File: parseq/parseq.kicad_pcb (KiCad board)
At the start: 2 copper layers, 47.5 x 55 mm, 46 parts, among them J1 Conn_01x01, J2 Conn_01x01, J3 Conn_01x01, J4 Conn_01x01, U1 Opamp_Quad, U2 Opamp_Dual

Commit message: .
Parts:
- moved R18 14.5 mm to (159.5, 102.5), turned to 90 degrees
- moved R19 8.33 mm to (140.4, 79.2), turned to -90 degrees
- moved RV3 0.15 mm to (178.5, 89.5)
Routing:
- net Net-(R18-Pad2): track 60.6 -> 26.2 mm
- net Net-(C7-Pad1): track 95.7 -> 64.9 mm
- net Net-(C11-Pad2): track 37.0 -> 25.8 mm
- net GND: track 0.00 -> 7.43 mm
- net Net-(C11-Pad1): track 7.64 -> 13.2 mm
- net Net-(U1B-+): track 36.9 -> 39.6 mm
- net Net-(C8-Pad1): track 8.20 -> 10.7 mm
- net Net-(U1C--): track 61.8 -> 64.2 mm
- net Net-(R17-Pad1): track 33.1 -> 31.4 mm
- net Net-(C12-Pad1): track 22.4 -> 23.2 mm
- net Net-(C9-Pad1): track 42.3 -> 41.7 mm
- net Net-(RV1A-6): track 41.3 -> 41.8 mm

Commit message: update board
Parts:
- removed R14: 100, 1_trevortjes_lib:R_1x4
- added C13: 100u, 1_trevortjes_lib:CP_ELCO_1x2_S, F.Cu at (141.6, 84.7)
- added R22: 100, 1_trevortjes_lib:R_1x4, F.Cu at (154.7, 76.8)
- added R23: 100, 1_trevortjes_lib:R_1x4, F.Cu at (156.2, 83.9)
- C2: moved to B.Cu
- C8: moved to F.Cu
- moved R15 44.3 mm to (155.1, 62.9), turned to 0 degrees
- moved J4 36.6 mm to (180.8, 77.4)
- moved R10 36.0 mm to (167.6, 111.5), turned to 90 degrees
- moved R16 28.5 mm to (163.8, 90.5), turned to 180 degrees
- moved R11 27.7 mm to (145.7, 106.8), turned to 180 degrees
- moved R17 26.2 mm to (137.0, 76.8)
- moved C2 24.8 mm to (150.8, 89.4), turned to 0 degrees
- moved J3 24.2 mm to (137.6, 89.8), turned to 180 degrees
- moved R4 23.5 mm to (155.3, 106.8), turned to 0 degrees
- moved R18 23.4 mm to (152.6, 80.2), turned to 0 degrees
- moved C8 23.1 mm to (149.8, 80.2), turned to 180 degrees
- moved R1 21.5 mm to (156.2, 87.1)
- moved R13 20.7 mm to (172.2, 106.8), turned to 0 degrees
- moved C6 20.6 mm to (175.0, 78.6)
- moved U1 20.6 mm to (169.8, 78.6)
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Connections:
- C5 pad 1: Net-(U1A-+) -> Net-(U1C-+)
- C5 pad 2: Net-(U1B-+) -> Net-(U1B--)
- C7 pad 2: Net-(U1A--) -> Net-(U1C--)
- R10 pad 2: Net-(U1A--) -> Net-(U1C--)
- R11 pad 1: Net-(U1C--) -> Net-(U1A-+)
- R13 pad 2: Net-(U1C-+) -> Net-(U1A--)
- R15 pad 1: Net-(U1E-V+) -> Net-(D1-K)
- R4 pad 1: Net-(U1C--) -> Net-(U1A-+)
- R4 pad 2: Net-(U1A-+) -> Net-(U1C-+)
- R5 pad 1: Net-(U1C-+) -> Net-(U1A--)
- R6 pad 1: Net-(U1C-+) -> Net-(U1A--)
- R7 pad 2: Net-(U1B-+) -> Net-(U1B--)
- R9 pad 1: Net-(U1A--) -> Net-(U1C--)
- RV1 pad 6: Net-(U1A-+) -> Net-(U1C-+)
- RV3 pad 3: Net-(U1C--) -> Net-(U1A-+)
- U1 pad 1: Net-(C7-Pad1) -> Net-(RV1A-6)
- U1 pad 5: Net-(U1B-+) -> /vref
- U1 pad 6: /vref -> Net-(U1B--)
- U1 pad 7: Net-(U1A-+) -> Net-(U1C-+)
- U1 pad 8: Net-(RV1A-6) -> Net-(C7-Pad1)
- U2 pad 8: Net-(U1E-V+) -> Net-(U2C-V+)
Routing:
- net Net-(U1C--): track 64.2 -> 21.7 mm
- net Net-(U1A-+): track 38.7 -> 80.0 mm
- net Net-(U1B-+): track 39.6 -> 0.00 mm
- net Net-(J4-Pin_1): track 42.2 -> 6.78 mm
- net Net-(C12-Pad1): track 23.2 -> 52.3 mm
- net Net-(R17-Pad1): track 31.4 -> 7.01 mm
- net Net-(D1-K): track 3.07 -> 26.7 mm
- net Net-(U1E-V+): track 32.1 -> 11.4 mm
- net Net-(R18-Pad2): track 26.2 -> 6.94 mm
- net Net-(C7-Pad1): track 64.9 -> 83.2 mm
- net Net-(J3-Pin_1): track 3.56 -> 17.1 mm
- net Net-(RV1A-6): track 41.8 -> 54.6 mm
- net Net-(U2C-V+): track 0.00 -> 12.1 mm
- net Net-(U1B--): track 0.00 -> 12.1 mm
- net Net-(C11-Pad2): track 25.8 -> 17.5 mm
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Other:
- board size 47.5 x 55 mm -> 47.5 x 54.6 mm
- board text added: "125b between screws (in long dimension)"

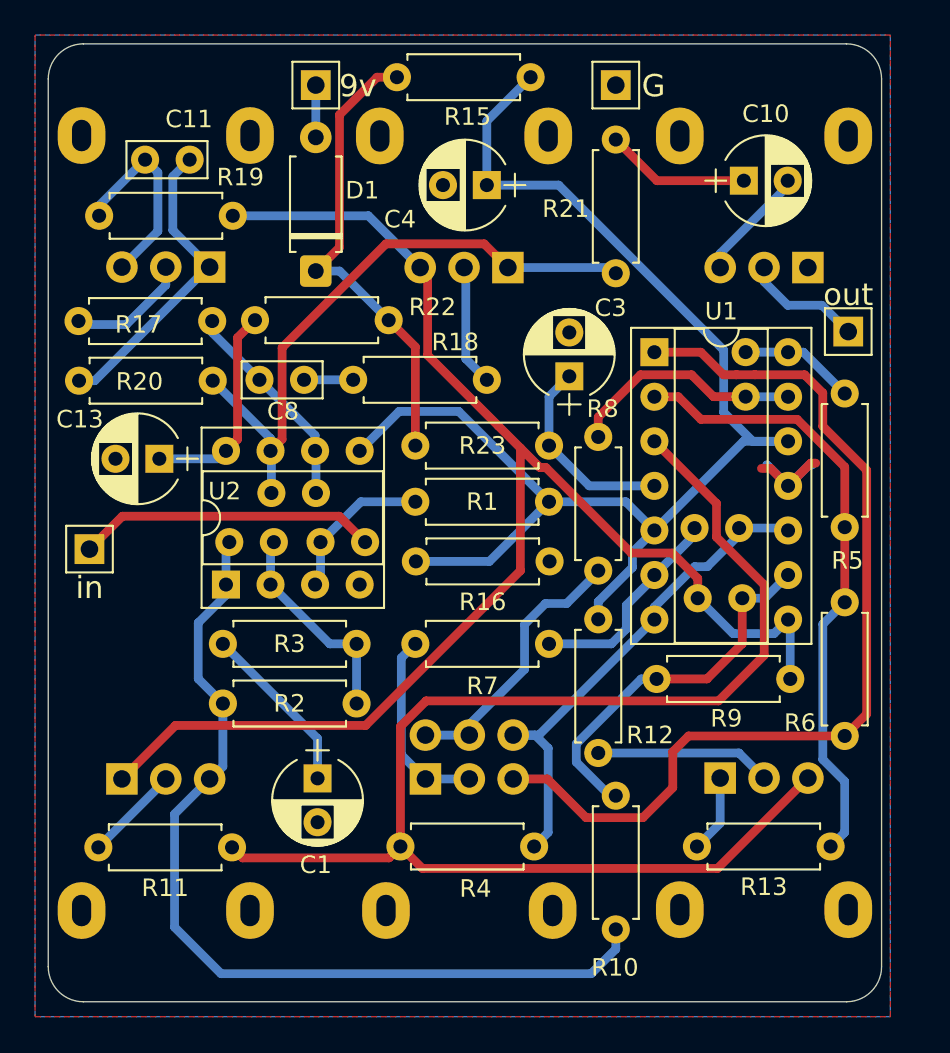
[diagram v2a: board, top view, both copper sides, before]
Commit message: shorter tracks
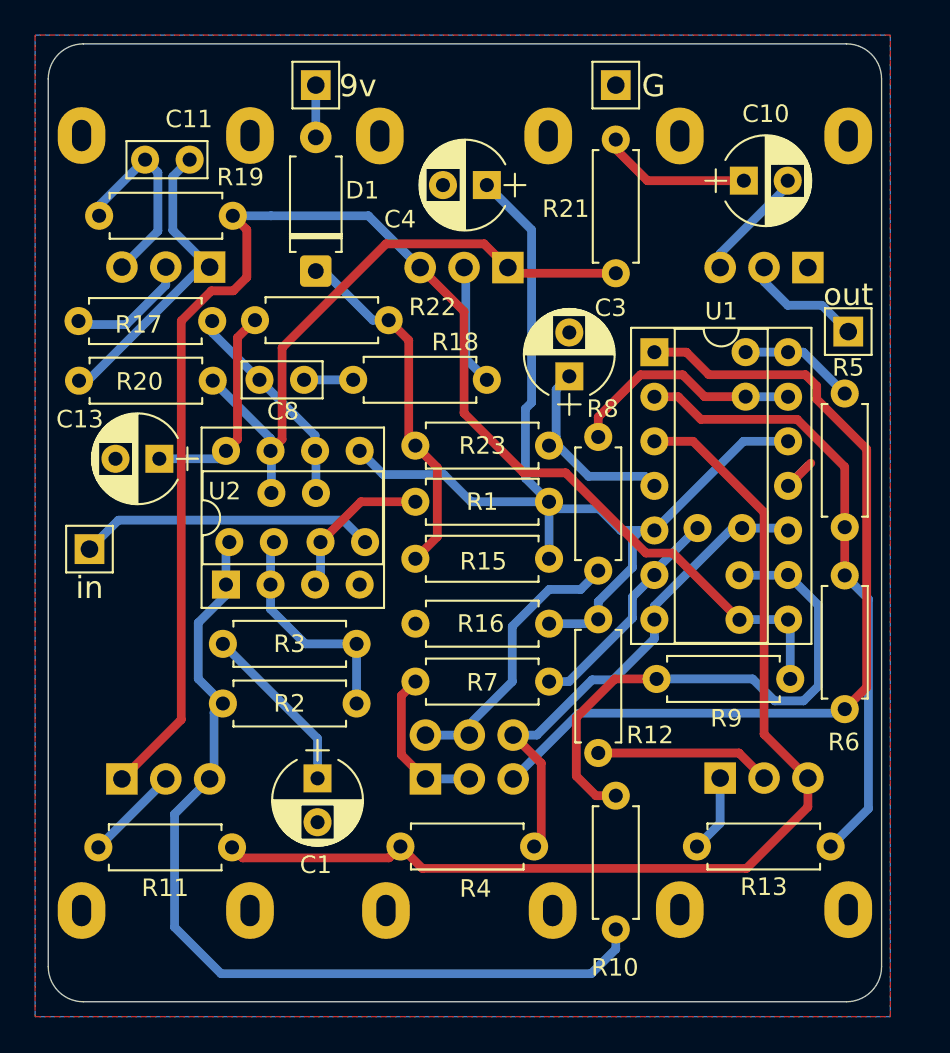
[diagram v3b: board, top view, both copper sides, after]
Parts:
- moved R15 27.5 mm to (156.2, 90.3)
- moved R16 8.43 mm to (156.2, 94.0), turned to 0 degrees
- moved C7 2.68 mm to (174.7, 93.8), turned to 90 degrees
- moved R7 2.15 mm to (156.2, 97.3)
- moved R6 1.53 mm to (180.7, 91.3)
- moved C5 0.17 mm to (174.8, 88.6)
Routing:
- net Net-(U1A-+): track 80.0 -> 61.1 mm
- net /vref: track 78.1 -> 61.2 mm
- net Net-(U1C--): track 21.7 -> 31.5 mm
- net Net-(D1-K): track 26.7 -> 20.6 mm
- net GND: track 7.64 -> 3.52 mm
- net Net-(RV1A-6): track 54.6 -> 50.7 mm
- net Net-(RV1A-4): track 11.1 -> 8.95 mm
- net Net-(C7-Pad1): track 83.2 -> 84.2 mm
- net Net-(U2A--): track 12.2 -> 13.0 mm
- net Net-(U1B--): track 12.1 -> 12.9 mm
- net Net-(U1C-+): track 29.5 -> 28.9 mm

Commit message: add name and version to silkscreen
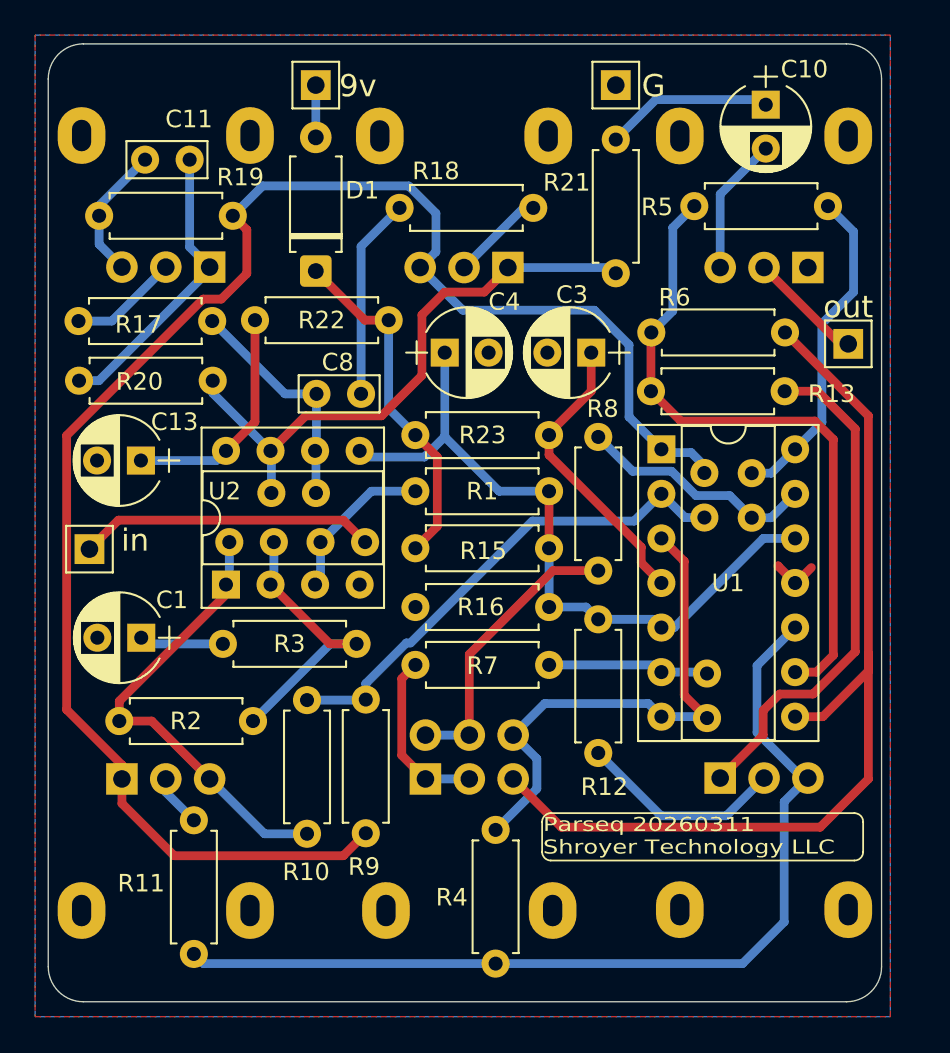
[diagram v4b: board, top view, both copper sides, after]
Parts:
- moved R13 26.4 mm to (177.2, 80.8), turned to 180 degrees
- moved R5 20.2 mm to (172.1, 70.2), turned to 0 degrees
- moved R10 18.4 mm to (150.0, 106.0)
- moved R6 17.7 mm to (169.6, 77.5), turned to 0 degrees
- moved R9 16.6 mm to (153.3, 98.4), turned to -90 degrees
- moved C1 12.9 mm to (140.6, 94.8), turned to 180 degrees
- moved C5 11.0 mm to (172.8, 99.4), turned to 90 degrees
- moved R18 10.2 mm to (155.3, 70.3)
- moved C4 9.85 mm to (157.8, 78.6), turned to 0 degrees
- moved C7 8.61 mm to (172.7, 85.5), turned to -90 degrees
- moved R4 8.60 mm to (160.8, 113.4), turned to 90 degrees
- moved C6 6.91 mm to (175.3, 85.5)
- moved R11 6.45 mm to (143.6, 112.9), turned to 90 degrees
- moved R2 5.99 mm to (146.9, 99.6)
- moved U1 5.55 mm to (170.2, 84.1)
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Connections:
- C5 pad 1: Net-(U1C-+) -> Net-(U1A-+)
- C7 pad 2: Net-(U1C--) -> Net-(U1A--)
- R10 pad 2: Net-(U1C--) -> Net-(U1A--)
- R11 pad 1: Net-(U1A-+) -> Net-(U1C-+)
- R13 pad 2: Net-(U1A--) -> Net-(U1C--)
- R4 pad 1: Net-(U1A-+) -> Net-(U1C-+)
- R4 pad 2: Net-(U1C-+) -> Net-(U1A-+)
- R5 pad 1: Net-(U1A--) -> Net-(U1C--)
- R6 pad 1: Net-(U1A--) -> Net-(U1C--)
- R9 pad 1: Net-(U1C--) -> Net-(U1A--)
- RV1 pad 6: Net-(U1C-+) -> Net-(U1A-+)
- RV3 pad 3: Net-(U1A-+) -> Net-(U1C-+)
- U1 pad 1: Net-(RV1A-6) -> Net-(C7-Pad1)
- U1 pad 7: Net-(U1C-+) -> Net-(U1A-+)
- U1 pad 8: Net-(C7-Pad1) -> Net-(RV1A-6)
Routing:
- net Net-(U1A-+): track 61.1 -> 30.4 mm
- net Net-(C12-Pad1): track 52.3 -> 26.2 mm
- net Net-(U1C-+): track 28.9 -> 54.5 mm
- net Net-(R13-Pad1): track 4.45 -> 29.1 mm
- net /vref: track 61.2 -> 40.7 mm
- net Net-(C6-Pad1): track 6.63 -> 18.9 mm
- net Net-(C7-Pad1): track 84.2 -> 95.8 mm
- net Net-(C8-Pad1): track 2.80 -> 11.5 mm
- net Net-(U1A--): track 35.6 -> 28.6 mm
- net Net-(U1C--): track 31.5 -> 38.0 mm
- net Net-(RV1A-6): track 50.7 -> 56.2 mm
- net Net-(U1E-V+): track 11.4 -> 16.8 mm
- net Net-(C1-Pad1): track 9.90 -> 4.80 mm
- net Net-(C11-Pad1): track 11.6 -> 7.75 mm
- net Net-(U1B--): track 12.9 -> 9.20 mm
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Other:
- board text added: "Parseq 20260311 Shroyer Technology LLC"

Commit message: snapshot
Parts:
- moved C6 1.42 mm to (175.4, 84.0)
- moved C7 1.42 mm to (172.7, 84.0)
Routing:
- net Net-(C11-Pad1): track 7.75 -> 10.5 mm
- net Net-(U1D--): track 13.7 -> 12.6 mm
- net Net-(C11-Pad2): track 16.8 -> 17.4 mm
- net Net-(C6-Pad1): track 18.9 -> 18.3 mm
- net Net-(C7-Pad1): track 95.8 -> 96.3 mm
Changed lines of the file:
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@@
 	(footprint "1_trevortjes_lib:C_CERAMIC_1x2"
 		(layer "B.Cu")
-		(at 172.65 85.46 -90)
+		(at 172.7 84.04 -90)
 		(tags "C capacitor std")
 		(property "Reference" "C7"
@@
 	(footprint "1_trevortjes_lib:C_CERAMIC_1x2"
 		(layer "B.Cu")
-		(at 175.35 85.47 -90)
+		(at 175.4 84.05 -90)
 		(tags "C capacitor std")
 		(property "Reference" "C6"
@@
 	)
 	(segment
-		(start 175.35 85.47)
-		(end 176.46 85.47)
+		(start 177.82 84.11)
+		(end 179.35 82.58)
 		(width 0.5)
 		(layer "B.Cu")
@@
 	)
 	(segment
-		(start 176.46 85.47)
+		(start 177.76 84.05)
 		(end 177.82 84.11)
 		(width 0.5)
@@
 	)
 	(segment
-		(start 177.82 84.11)
-		(end 179.35 82.58)
+		(start 179.35 82.58)
+		(end 179.35 76.95)
 		(width 0.5)
 		(layer "B.Cu")
@@
 	)
 	(segment
-		(start 179.35 82.58)
-		(end 179.35 76.95)
+		(start 175.4 84.05)
+		(end 177.76 84.05)
 		(width 0.5)
 		(layer "B.Cu")
@@
 	)
 	(segment
-		(start 175.35 88.01)
-		(end 176.46 88.01)
+		(start 171.451 85.361)
+		(end 168.556 85.361)
 		(width 0.5)
 		(layer "B.Cu")
@@
 	)
 	(segment
-		(start 168.556 85.361)
-		(end 170.781818 85.361)
+		(start 175.4 86.59)
+		(end 174.139 85.329)
 		(width 0.5)
 		(layer "B.Cu")
@@
 	)
 	(segment
-		(start 170.781818 85.361)
-		(end 172.169818 86.749)
+		(start 171.483 85.329)
+		(end 171.451 85.361)
 		(width 0.5)
 		(layer "B.Cu")
@@
 	)
 	(segment
-		(start 166.6 83.405)
-		(end 168.556 85.361)
+		(start 174.139 85.329)
+		(end 171.483 85.329)
 		(width 0.5)
 		(layer "B.Cu")
@@
 	)
 	(segment
-		(start 176.46 88.01)
+		(start 177.76 86.59)
 		(end 177.82 86.65)
 		(width 0.5)
@@
 	)
 	(segment
-		(start 172.169818 86.749)
-		(end 174.089 86.749)
+		(start 168.556 85.361)
+		(end 166.6 83.405)
 		(width 0.5)
 		(layer "B.Cu")
@@
 	)
 	(segment
-		(start 174.089 86.749)
-		(end 175.35 88.01)
+		(start 175.4 86.59)
+		(end 177.76 86.59)
 		(width 0.5)
 		(layer "B.Cu")
@@
 	)
 	(segment
-		(start 145.77 70.8)
-		(end 147.471 69.099)
+		(start 156.55 73.65)
+		(end 156.45 73.75)
 		(width 0.5)
 		(layer "B.Cu")
@@
 	)
 	(segment
-		(start 157.35 70.655818)
-		(end 157.35 72.85)
+		(start 157.6315 76.1815)
+		(end 166.3815 76.1815)
 		(width 0.5)
 		(layer "B.Cu")
@@
 	)
 	(segment
-		(start 157.35 72.85)
-		(end 156.45 73.75)
+		(start 168.354 82.264)
+		(end 170.2 84.11)
 		(width 0.5)
 		(layer "B.Cu")
@@
 	)
 	(segment
-		(start 171.9 84.3)
-		(end 170.39 84.3)
+		(start 156.9 69.35)
+		(end 156.9 71.6)
 		(width 0.5)
 		(layer "B.Cu")
@@
 	)
 	(segment
-		(start 168.354 82.264)
-		(end 170.2 84.11)
+		(start 166.3815 76.1815)
+		(end 168.354 78.154)
 		(width 0.5)
 		(layer "B.Cu")
@@
 	)
 	(segment
-		(start 155.793182 69.099)
-		(end 157.35 70.655818)
+		(start 152.6 68.65)
+		(end 156.2 68.65)
 		(width 0.5)
 		(layer "B.Cu")
@@
 	)
 	(segment
-		(start 156.45 73.75)
-		(end 158.8815 76.1815)
+		(start 156.45 75)
+		(end 157.6315 76.1815)
 		(width 0.5)
 		(layer "B.Cu")
@@
 	)
 	(segment
-		(start 170.39 84.3)
-		(end 170.2 84.11)
+		(start 145.77 70.8)
+		(end 150.45 70.8)
 		(width 0.5)
 		(layer "B.Cu")
@@
 	)
 	(segment
-		(start 158.8815 76.1815)
-		(end 166.3815 76.1815)
+		(start 156.9 71.6)
+		(end 156.55 71.95)
 		(width 0.5)
 		(layer "B.Cu")
@@
 	)
 	(segment
-		(start 172.65 85.05)
-		(end 171.9 84.3)
+		(start 156.45 73.75)
+		(end 156.45 75)
 		(width 0.5)
 		(layer "B.Cu")
@@
 	)
 	(segment
-		(start 166.3815 76.1815)
-		(end 168.354 78.154)
+		(start 172.63 84.11)
+		(end 172.7 84.04)
+		(width 0.5)
+		(layer "B.Cu")
+		(net 8)
+	)
+	(segment
+		(start 156.2 68.65)
+		(end 156.9 69.35)
 		(width 0.5)
 		(layer "B.Cu")
@@
 	)
 	(segment
-		(start 147.471 69.099)
-		(end 155.793182 69.099)
+		(start 170.2 84.11)
+		(end 172.63 84.11)
 		(width 0.5)
 		(layer "B.Cu")
@@
 	)
 	(segment
-		(start 172.65 85.46)
-		(end 172.65 85.05)
+		(start 156.55 71.95)
+		(end 156.55 73.65)
+		(width 0.5)
+		(layer "B.Cu")
+		(net 8)
+	)
+	(segment
+		(start 150.45 70.8)
+		(end 152.6 68.65)
 		(width 0.5)
 		(layer "B.Cu")
@@
 	)
 	(segment
-		(start 143.31 72.585)
+		(start 143.875 73.725)
 		(end 144.45 73.725)
 		(width 0.5)
@@
 	)
 	(segment
-		(start 138.13637 80.2)
-		(end 144.45 73.88637)
+		(start 137.005 80.2)
+		(end 137.4 80.2)
+		(width 0.5)
+		(layer "B.Cu")
+		(net 13)
+	)
+	(segment
+		(start 142.45 71.725)
+		(end 144.45 73.725)
 		(width 0.5)
 		(layer "B.Cu")
@@
 	)
 	(segment
-		(start 137.005 80.2)
-		(end 138.13637 80.2)
+		(start 137.4 80.2)
+		(end 143.875 73.725)
 		(width 0.5)
 		(layer "B.Cu")
@@
 	(segment
 		(start 143.31 67.6)
-		(end 143.31 72.585)
+		(end 143.31 67.79)
 		(width 0.5)
 		(layer "B.Cu")
@@
 	)
 	(segment
-		(start 144.45 73.88637)
-		(end 144.45 73.725)
+		(start 143.31 67.79)
+		(end 142.45 68.65)
+		(width 0.5)
+		(layer "B.Cu")
+		(net 13)
+	)
+	(segment
+		(start 142.45 68.65)
+		(end 142.45 71.725)
 		(width 0.5)
 		(layer "B.Cu")
@@
 	)
 	(segment
-		(start 138.15 70.22)
+		(start 141.25 68.08)
 		(end 140.77 67.6)
 		(width 0.5)
@@
 	)
 	(segment
-		(start 138.15 70.8)
-		(end 138.15 70.22)
+		(start 139.45 72.85)
+		(end 141.25 71.05)
+		(width 0.5)
+		(layer "B.Cu")
+		(net 14)
+	)
+	(segment
+		(start 141.25 71.05)
+		(end 141.25 68.08)
 		(width 0.5)
 		(layer "B.Cu")
@@
 	)
 	(segment
+		(start 139.45 73.725)
+		(end 139.45 72.85)
+		(width 0.5)
+		(layer "B.Cu")
+		(net 14)
+	)
+	(segment
 		(start 138.15 70.8)
 		(end 138.15 72.425)
@@
 	)
 	(segment
-		(start 172.65 88)
-		(end 171.55 88)
+		(start 170.2 86.65)
+		(end 172.63 86.65)
 		(width 0.5)
 		(layer "B.Cu")
@@
 	)
 	(segment
+		(start 172.63 86.65)
+		(end 172.7 86.58)
+		(width 0.5)
+		(layer "B.Cu")
+		(net 18)
+	)
+	(segment
 		(start 168.65 88.2)
 		(end 162.849182 88.2)
@@
 	)
 	(segment
-		(start 171.55 88)
-		(end 170.2 86.65)
-		(width 0.5)
-		(layer "B.Cu")
-		(net 18)
-	)
-	(segment
 		(start 170.2 96.81)
 		(end 172.72 96.81)
@@
 	)
 	(segment
-		(start 176 99)
-		(end 176.939 98.061)
+		(start 179.1 80.8)
+		(end 177.225 80.8)
 		(width 0.5)
 		(layer "F.Cu")
@@
 	)
 	(segment
-		(start 181.25 82.95)
-		(end 179.1 80.8)
+		(start 173.55 102.85)
+		(end 176 100.4)
 		(width 0.5)
 		(layer "F.Cu")
@@
 	)
 	(segment
-		(start 178.839 98.061)
-		(end 181.25 95.65)
+		(start 181 95.9)
+		(end 181 82.7)
 		(width 0.5)
 		(layer "F.Cu")
@@
 	)
 	(segment
-		(start 176 100.4)
-		(end 176 99)
+		(start 176.939 98.061)
+		(end 178.839 98.061)
 		(width 0.5)
 		(layer "F.Cu")
@@
 	)
 	(segment
-		(start 181.25 95.65)
-		(end 181.25 82.95)
+		(start 176 100.4)
+		(end 176 99)
 		(width 0.5)
 		(layer "F.Cu")
@@
 	)
 	(segment
-		(start 179.1 80.8)
-		(end 177.225 80.8)
+		(start 178.839 98.061)
+		(end 181 95.9)
 		(width 0.5)
 		(layer "F.Cu")
@@
 	)
 	(segment
-		(start 173.55 102.85)
-		(end 176 100.4)
+		(start 176 99)
+		(end 176.939 98.061)
 		(width 0.5)
 		(layer "F.Cu")
@@
 	)
 	(segment
-		(start 176.939 98.061)
-		(end 178.839 98.061)
+		(start 181 82.7)
+		(end 179.1 80.8)
 		(width 0.5)
 		(layer "F.Cu")
@@
 	)
 	(segment
+		(start 141.95 74.2)
+		(end 141.95 73.725)
+		(width 0.5)
+		(layer "B.Cu")
+		(net 28)
+	)
+	(segment
 		(start 136.975 76.8)
-		(end 138.875 76.8)
+		(end 139.35 76.8)
 		(width 0.5)
 		(layer "B.Cu")
@@
 	)
 	(segment
-		(start 138.875 76.8)
-		(end 141.95 73.725)
+		(start 139.35 76.8)
+		(end 141.95 74.2)
 		(width 0.5)
 		(layer "B.Cu")
